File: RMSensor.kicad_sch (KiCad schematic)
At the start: 26 parts, among them J1 Conn_01x02, J2 Conn_01x02, J3 Conn_01x04, U1 OPA209AID, U2 OPA2350UA, U3 MC78L05_TO92, U4 TLE2425xD

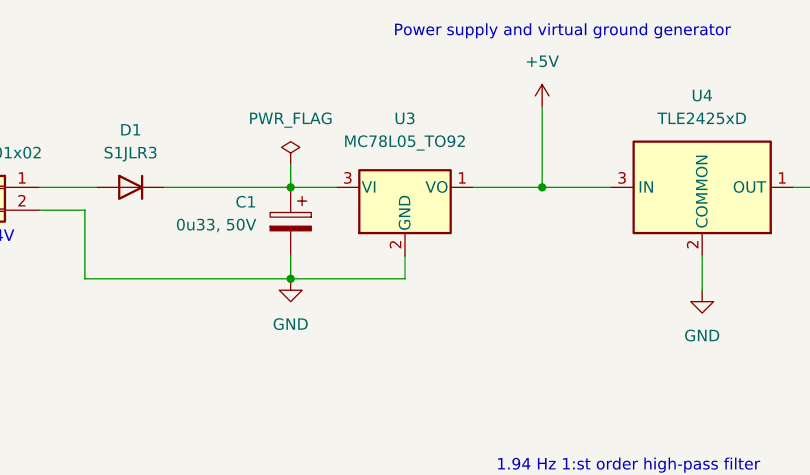
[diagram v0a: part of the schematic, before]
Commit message: changed res and cap footprint to 805 and changed regulator
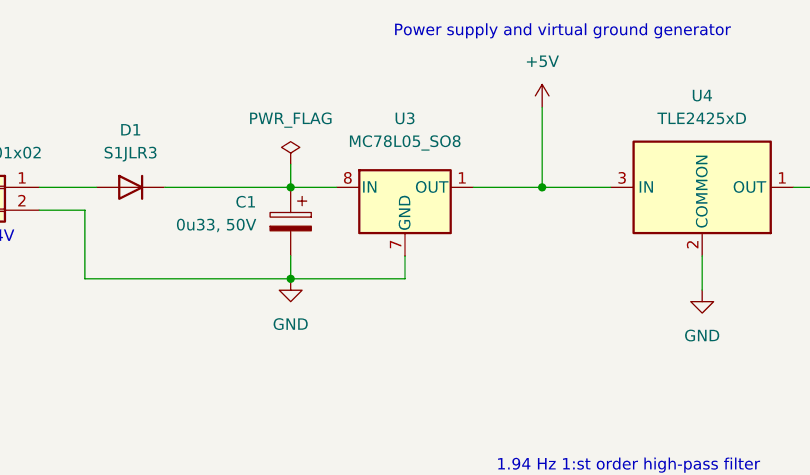
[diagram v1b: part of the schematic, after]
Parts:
- removed U3: MC78L05_TO92, Package_TO_SOT_THT:TO-92_Inline, symbol Regulator_Linear:MC78L05_TO92
- added U3: MC78L05_SO8, Package_SO:SOIC-8_3.9x4.9mm_P1.27mm, symbol Regulator_Linear:MC78L05_SO8
- C1, C10, C2, C3, C4, C5, C6, C7, C8: footprint Capacitor_SMD:C_1206_3216Metric -> Capacitor_SMD:C_0805_2012Metric
- R1, R2, R3, R4, R5, R6, R7, R8, R9: footprint Resistor_SMD:R_1206_3216Metric -> Resistor_SMD:R_0805_2012Metric
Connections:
- net +5V: now also U3.1 (OUT)
- net GND: now also U3.2 (GND), U3.3 (GND), U3.6 (GND), U3.7 (GND)
- net at C1.1, D1.1 (K): now also U3.8 (IN)

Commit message: pcb with traces
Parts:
- C2, C8: value 100n -> 1u
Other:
- note removed: "De-coupling capacitors"
- moved on the sheet: C10, C2, C7, C8
